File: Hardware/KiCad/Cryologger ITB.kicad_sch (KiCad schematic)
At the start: 16 parts, among them J1 Screw_Terminal_01x02, U1 Adafruit_LSM303AGR, U2 Pololu_D36V6x, U6 Adafruit_BME280, U8 RockBLOCK_Footprint, U9 Pololu_D36V6x

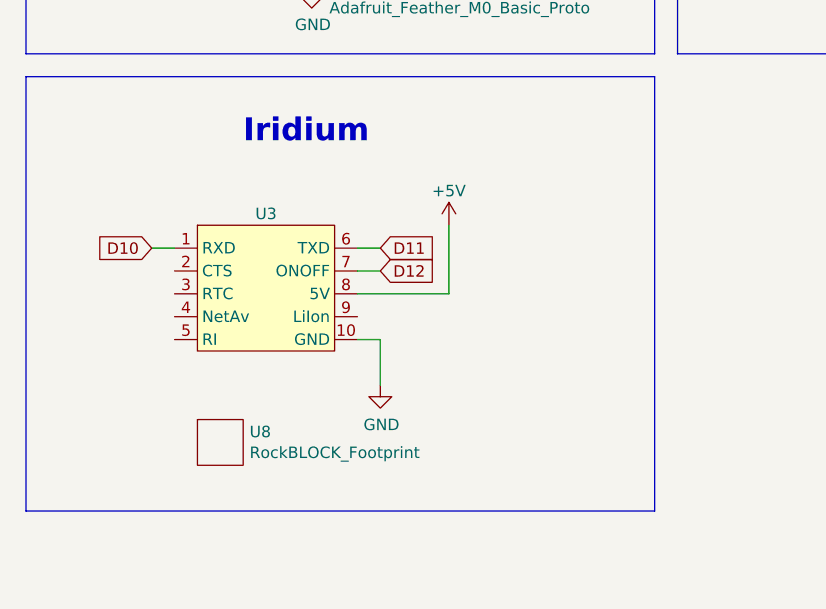
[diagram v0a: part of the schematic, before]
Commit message: Add N-MOSFET and to control on/off logic of RockBLOCK v3.F
Added a jumper to ensure N-MOSFET is backwards compatible. Updated files to KiCad 8.0.
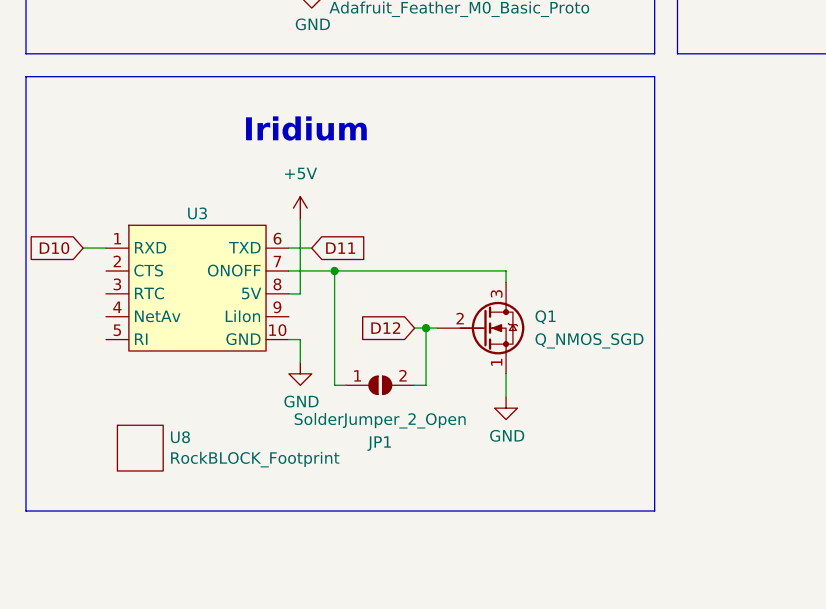
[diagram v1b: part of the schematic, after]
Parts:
- added JP1: SolderJumper_2_Open, Jumper:SolderJumper-2_P1.3mm_Open_RoundedPad1.0x1.5mm, symbol Jumper:SolderJumper_2_Open
- added Q1: Q_NMOS_SGD, Package_TO_SOT_THT:TO-92, symbol Device:Q_NMOS_SGD
- U6: footprint Cryologger:Adafruit_DPS310 -> Cryologger:Adafruit_BME280
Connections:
- net D12: now also JP1.2 (B), Q1.2 (G); no longer U3.7 (ONOFF)
- net GND: now also Q1.1 (S)
- new net: JP1.1 (A), Q1.3 (D), U3.7 (ONOFF)
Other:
- moved on the sheet: U3, U8

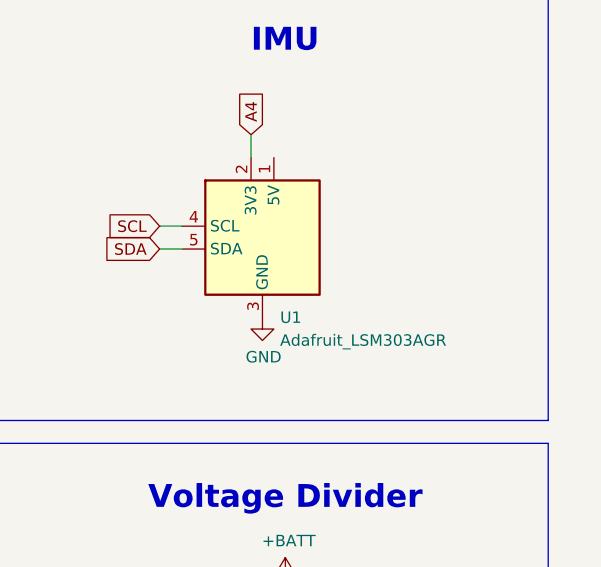
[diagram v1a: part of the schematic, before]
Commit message: Add N-MOSFET to PCB to control RockBLOCK v3.F
Updated KiCad files. Added Creative Commons license.
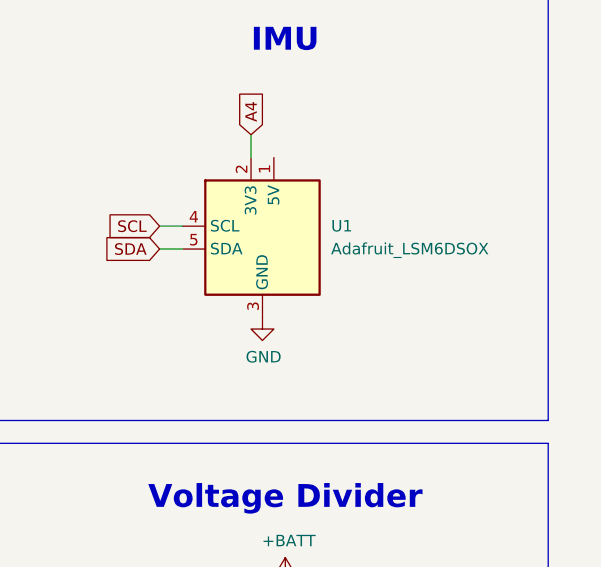
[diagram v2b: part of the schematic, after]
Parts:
- removed U1: Adafruit_LSM303AGR, Cryologger:Adafruit_LSM303AGR, symbol Cryologger:Adafruit_LSM303AGR
- added U1: Adafruit_LSM6DSOX, Cryologger:Adafruit_LSM6DS0X, symbol Cryologger:Adafruit_LSM6DSOX
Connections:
- net A4: now also U1.2 (3V3)
- net GND: now also U1.3 (GND)
- net SCL: now also U1.4 (SCL)
- net SDA: now also U1.5 (SDA)
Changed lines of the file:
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@@
 	(title_block
 		(title "Cryologger Ice Tracking Beacon")
-		(date "2023-03-05")
-		(rev "3.1")
+		(date "2024-05-01")
+		(rev "3.2")
+		(comment 1 "© 2024. This work is openly licensed via CC BY-NC-SA 4.0.")
+		(comment 2 "Designed by: Adam Garbo")
 	)
 	(junction
@@
 	)
 	(symbol
+		(lib_id "Cryologger:Adafruit_LSM6DSOX")
+		(at 251.46 41.91 0)
+		(unit 1)
+		(exclude_from_sim no)
+		(in_bom yes)
+		(on_board yes)
+		(dnp no)
+		(fields_autoplaced yes)
+		(property "Reference" "U1"
+			(at 259.08 40.6399 0)
+			(effects
+				(font
+					(size 1.27 1.27)
+				)
+				(justify left)
+			)
+		)
+		(property "Value" "Adafruit_LSM6DSOX"
+			(at 259.08 43.1799 0)
+			(effects
+				(font
+					(size 1.27 1.27)
+				)
+				(justify left)
+			)
+		)
+		(property "Footprint" "Cryologger:Adafruit_LSM6DS0X"
+			(at 251.46 41.91 0)
+			(effects
+				(font
+					(size 1.27 1.27)
+				)
+				(hide yes)
+			)
+		)
+		(property "Datasheet" ""
+			(at 251.46 41.91 0)
+			(effects
+				(font
+					(size 1.27 1.27)
+				)
+				(hide yes)
+			)
+		)
+		(property "Description" ""
+			(at 251.46 41.91 0)
+			(effects
+				(font
+					(size 1.27 1.27)
+				)
+				(hide yes)
+			)
+		)
+		(pin "4"
+		)
+		(pin "5"
+		)
+		(pin "3"
+		)
+		(pin "1"
+		)
+		(pin "2"
+		)
+		(instances
+			(project "Cryologger ITB"
+				(path "/ac73d61e-8e75-480c-9a5b-4c36169649bf"
+					(reference "U1")
+					(unit 1)
+				)
+			)
+		)
+	)
+	(symbol
 		(lib_id "Cryologger:Pololu_D36V6x")
 		(at 182.88 144.78 0)
@@
 					(unit 1)
 				)
-			)
-		)
-	)
-	(symbol
-		(lib_id "Cryologger:Adafruit_LSM303AGR")
-		(at 251.46 41.91 0)
-		(unit 1)
-		(exclude_from_sim no)
-		(in_bom yes)
-		(on_board yes)
-		(dnp no)
-		(fields_autoplaced yes)
-		(property "Reference" "U1"
-			(at 253.4159 50.8 0)
-			(effects
-				(font
-					(size 1.27 1.27)
-				)
-				(justify left)
-			)
-		)
-		(property "Value" "Adafruit_LSM303AGR"
-			(at 253.4159 53.34 0)
-			(effects
-				(font
-					(size 1.27 1.27)
-				)
-				(justify left)
-			)
-		)
-		(property "Footprint" "Cryologger:Adafruit_LSM303AGR"
-			(at 251.46 41.91 0)
-			(effects
-				(font
-					(size 1.27 1.27)
-				)
-				(hide yes)
-			)
-		)
-		(property "Datasheet" ""
-			(at 251.46 41.91 0)
-			(effects
-				(font
-					(size 1.27 1.27)
-				)
-				(hide yes)
-			)
-		)
-		(property "Description" ""
-			(at 251.46 41.91 0)
-			(effects
-				(font
-					(size 1.27 1.27)
-				)
-				(hide yes)
-			)
-		)
-		(pin "1"
-		)
-		(pin "2"
-		)
-		(pin "3"
-		)
-		(pin "4"
-		)
-		(pin "5"
-		)
-		(instances
-			(project "Cryologger ITB"
-				(path "/ac73d61e-8e75-480c-9a5b-4c36169649bf"
-					(reference "U1")
-					(unit 1)
-				)
